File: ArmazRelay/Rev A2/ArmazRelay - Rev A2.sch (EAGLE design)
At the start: 9 parts, among them J1 MSTBA2, J2 MSTBA3, J3 22-05-7038-03, J4 22-05-7038-03, K1 MY2, T1 EXMACHINA-LOGO-NAME

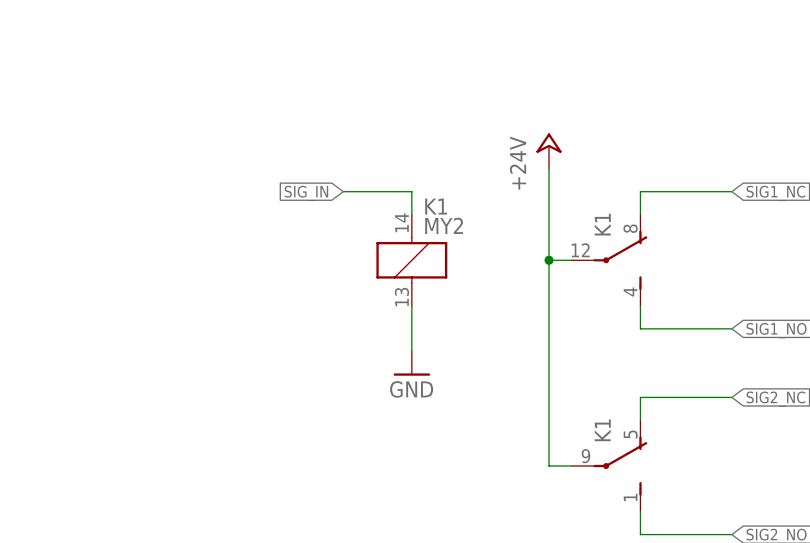
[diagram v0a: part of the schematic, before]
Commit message: Update relay package and add polarity on relay coil
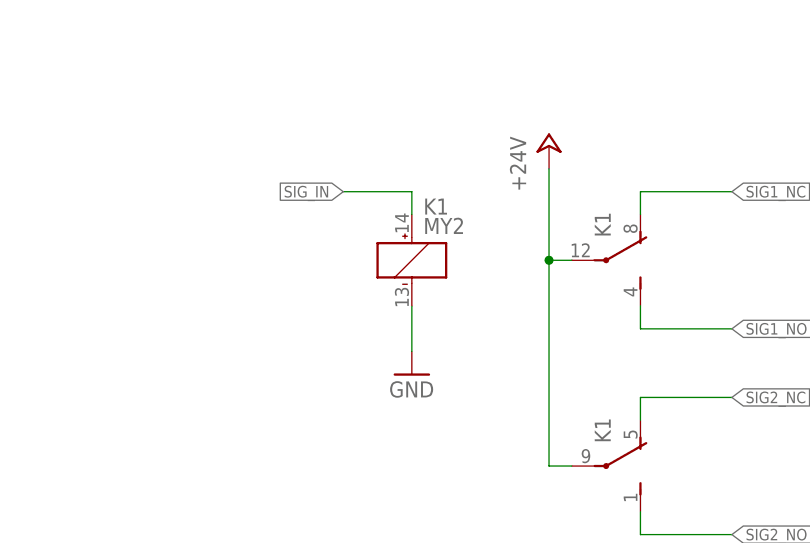
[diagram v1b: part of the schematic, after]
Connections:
- net GND: now also K1G$1.-; no longer K1G$1.COIL2
- net SIG_IN: now also K1G$1.+; no longer K1G$1.COIL1
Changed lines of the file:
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@@
 <grid distance="0.1" unitdist="inch" unit="inch" style="lines" multiple="1" display="no" altdistance="0.01" altunitdist="inch" altunit="inch"/>
 <layers>
-<layer number="1" name="Top" color="4" fill="1" visible="no" active="no"/>
-<layer number="2" name="Route2" color="1" fill="3" visible="no" active="no"/>
-<layer number="3" name="Route3" color="4" fill="3" visible="no" active="no"/>
-<layer number="14" name="Route14" color="1" fill="6" visible="no" active="no"/>
-<layer number="15" name="Route15" color="4" fill="6" visible="no" active="no"/>
-<layer number="16" name="Bottom" color="1" fill="1" visible="no" active="no"/>
-<layer number="17" name="Pads" color="2" fill="1" visible="no" active="no"/>
-<layer number="18" name="Vias" color="2" fill="1" visible="no" active="no"/>
-<layer number="19" name="Unrouted" color="6" fill="1" visible="no" active="no"/>
-<layer number="20" name="Dimension" color="15" fill="1" visible="no" active="no"/>
-<layer number="21" name="tPlace" color="7" fill="1" visible="no" active="no"/>
-<layer number="22" name="bPlace" color="7" fill="1" visible="no" active="no"/>
-<layer number="23" name="tOrigins" color="15" fill="1" visible="no" active="no"/>
-<layer number="24" name="bOrigins" color="15" fill="1" visible="no" active="no"/>
-<layer number="25" name="tNames" color="7" fill="1" visible="no" active="no"/>
-<layer number="26" name="bNames" color="7" fill="1" visible="no" active="no"/>
-<layer number="27" name="tValues" color="7" fill="1" visible="no" active="no"/>
-<layer number="28" name="bValues" color="7" fill="1" visible="no" active="no"/>
+<layer number="1" name="Top" color="4" fill="1" visible="yes" active="no"/>
+<layer number="2" name="Route2" color="1" fill="3" visible="yes" active="no"/>
+<layer number="3" name="Route3" color="4" fill="3" visible="yes" active="no"/>
+<layer number="14" name="Route14" color="1" fill="6" visible="yes" active="no"/>
+<layer number="15" name="Route15" color="4" fill="6" visible="yes" active="no"/>
+<layer number="16" name="Bottom" color="1" fill="1" visible="yes" active="no"/>
+<layer number="17" name="Pads" color="2" fill="1" visible="yes" active="no"/>
+<layer number="18" name="Vias" color="2" fill="1" visible="yes" active="no"/>
+<layer number="19" name="Unrouted" color="6" fill="1" visible="yes" active="no"/>
+<layer number="20" name="Dimension" color="15" fill="1" visible="yes" active="no"/>
+<layer number="21" name="tPlace" color="7" fill="1" visible="yes" active="no"/>
+<layer number="22" name="bPlace" color="7" fill="1" visible="yes" active="no"/>
+<layer number="23" name="tOrigins" color="15" fill="1" visible="yes" active="no"/>
+<layer number="24" name="bOrigins" color="15" fill="1" visible="yes" active="no"/>
+<layer number="25" name="tNames" color="7" fill="1" visible="yes" active="no"/>
+<layer number="26" name="bNames" color="7" fill="1" visible="yes" active="no"/>
+<layer number="27" name="tValues" color="7" fill="1" visible="yes" active="no"/>
+<layer number="28" name="bValues" color="7" fill="1" visible="yes" active="no"/>
 <layer number="29" name="tStop" color="7" fill="3" visible="no" active="no"/>
 <layer number="30" name="bStop" color="7" fill="6" visible="no" active="no"/>
@@
 <layer number="35" name="tGlue" color="7" fill="4" visible="no" active="no"/>
 <layer number="36" name="bGlue" color="7" fill="5" visible="no" active="no"/>
-<layer number="37" name="tTest" color="7" fill="1" visible="no" active="no"/>
-<layer number="38" name="bTest" color="7" fill="1" visible="no" active="no"/>
+<layer number="37" name="tTest" color="7" fill="1" visible="yes" active="no"/>
+<layer number="38" name="bTest" color="7" fill="1" visible="yes" active="no"/>
 <layer number="39" name="tKeepout" color="4" fill="11" visible="no" active="no"/>
 <layer number="40" name="bKeepout" color="1" fill="11" visible="no" active="no"/>
@@
 <layer number="44" name="Drills" color="7" fill="1" visible="no" active="no"/>
 <layer number="45" name="Holes" color="7" fill="1" visible="no" active="no"/>
-<layer number="46" name="Milling" color="3" fill="1" visible="no" active="no"/>
-<layer number="47" name="Measures" color="7" fill="1" visible="no" active="no"/>
-<layer number="48" name="Document" color="7" fill="1" visible="no" active="no"/>
-<layer number="49" name="Reference" color="7" fill="1" visible="no" active="no"/>
-<layer number="50" name="dxf" color="7" fill="1" visible="no" active="no"/>
-<layer number="51" name="tDocu" color="7" fill="1" visible="no" active="no"/>
-<layer number="52" name="bDocu" color="7" fill="1" visible="no" active="no"/>
-<layer number="53" name="tGND_GNDA" color="7" fill="1" visible="no" active="no"/>
-<layer number="54" name="bGND_GNDA" color="7" fill="1" visible="no" active="no"/>
-<layer number="56" name="wert" color="7" fill="1" visible="no" active="no"/>
+<layer number="46" name="Milling" color="3" fill="1" visible="yes" active="no"/>
+<layer number="47" name="Measures" color="7" fill="1" visible="yes" active="no"/>
+<layer number="48" name="Document" color="7" fill="1" visible="yes" active="no"/>
+<layer number="49" name="Reference" color="7" fill="1" visible="yes" active="no"/>
+<layer number="50" name="dxf" color="7" fill="1" visible="yes" active="no"/>
+<layer number="51" name="tDocu" color="7" fill="1" visible="yes" active="no"/>
+<layer number="52" name="bDocu" color="7" fill="1" visible="yes" active="no"/>
+<layer number="53" name="tGND_GNDA" color="7" fill="1" visible="yes" active="no"/>
+<layer number="54" name="bGND_GNDA" color="7" fill="1" visible="yes" active="no"/>
+<layer number="56" name="wert" color="7" fill="1" visible="yes" active="no"/>
 <layer number="90" name="Modules" color="5" fill="1" visible="no" active="yes"/>
 <layer number="91" name="Nets" color="2" fill="1" visible="yes" active="yes"/>
@@
 <instance part="J2" gate="-3" x="25.4" y="203.2"/>
 <instance part="K1" gate="G$2" x="162.56" y="218.44" rot="MR90"/>
-<instance part="K1" gate="G$1" x="142.24" y="218.44"/>
 <instance part="P+1" gate="1" x="35.56" y="220.98"/>
 <instance part="GND1" gate="1" x="35.56" y="198.12"/>
@@
 <instance part="J3" gate="-3" x="73.66" y="231.14" rot="MR0"/>
 <instance part="GND5" gate="1" x="86.36" y="228.6"/>
+<instance part="K1" gate="G$1" x="142.24" y="218.44"/>
 </instances>
 <busses>
@@
 </segment>
 <segment>
-<pinref part="K1" gate="G$1" pin="COIL2"/>
 <pinref part="GND3" gate="1" pin="GND"/>
 <wire x1="142.24" y1="213.36" x2="142.24" y2="208.28" width="0.1524" layer="91"/>
+<pinref part="K1" gate="G$1" pin="-"/>
 </segment>
 <segment>
@@
 <segment>
 <wire x1="134.62" y1="226.06" x2="142.24" y2="226.06" width="0.1524" layer="91"/>
-<pinref part="K1" gate="G$1" pin="COIL1"/>
 <wire x1="142.24" y1="226.06" x2="142.24" y2="223.52" width="0.1524" layer="91"/>
 <label x="134.62" y="226.06" size="1.27" layer="95" rot="R180" xref="yes"/>
+<pinref part="K1" gate="G$1" pin="+"/>
 </segment>
 </net>
